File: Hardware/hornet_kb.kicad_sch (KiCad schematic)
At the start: 28 parts, among them J1 Conn_ST_STDC14, J10 USB_C_Receptacle_USB2.0, SW98 SW_Push, U1 nRF52840, Y1 32.768kHz, Y2 32MHz

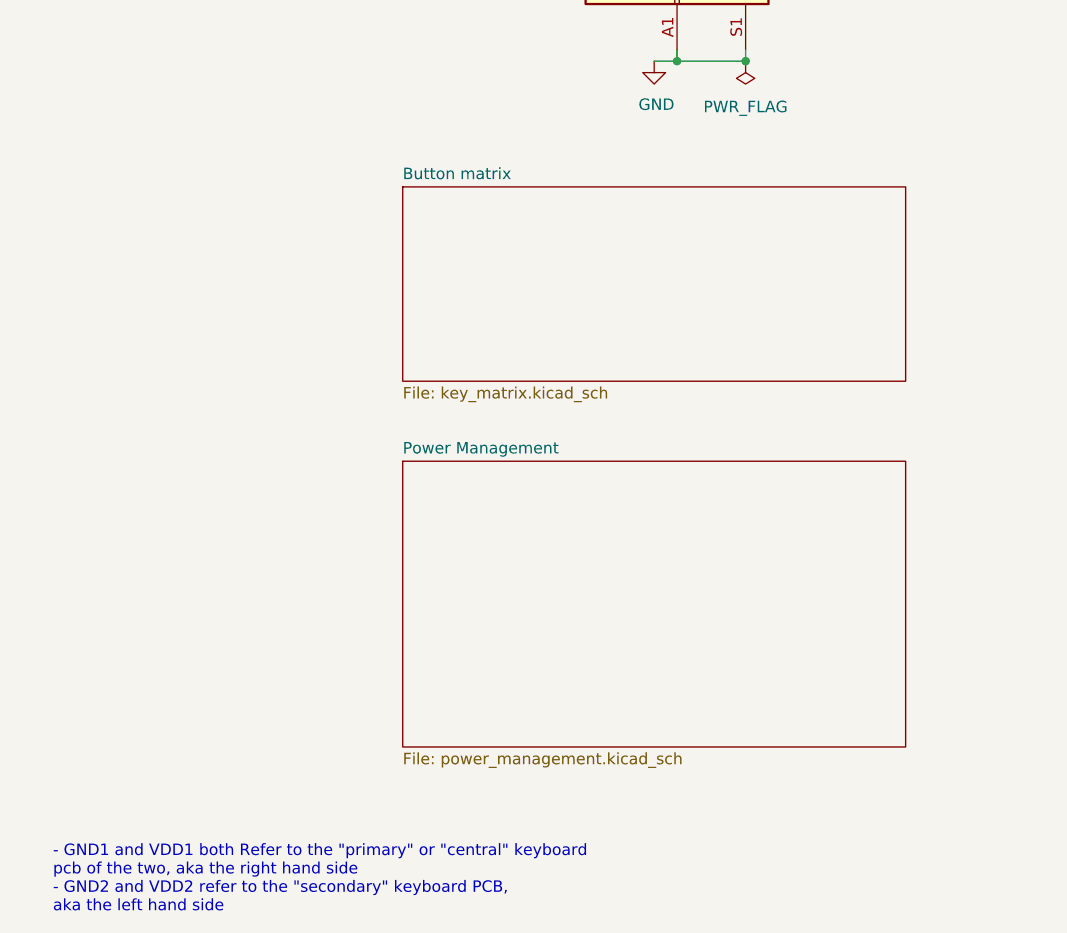
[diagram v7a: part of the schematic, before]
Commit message: Add higherarchical pins to key matrix
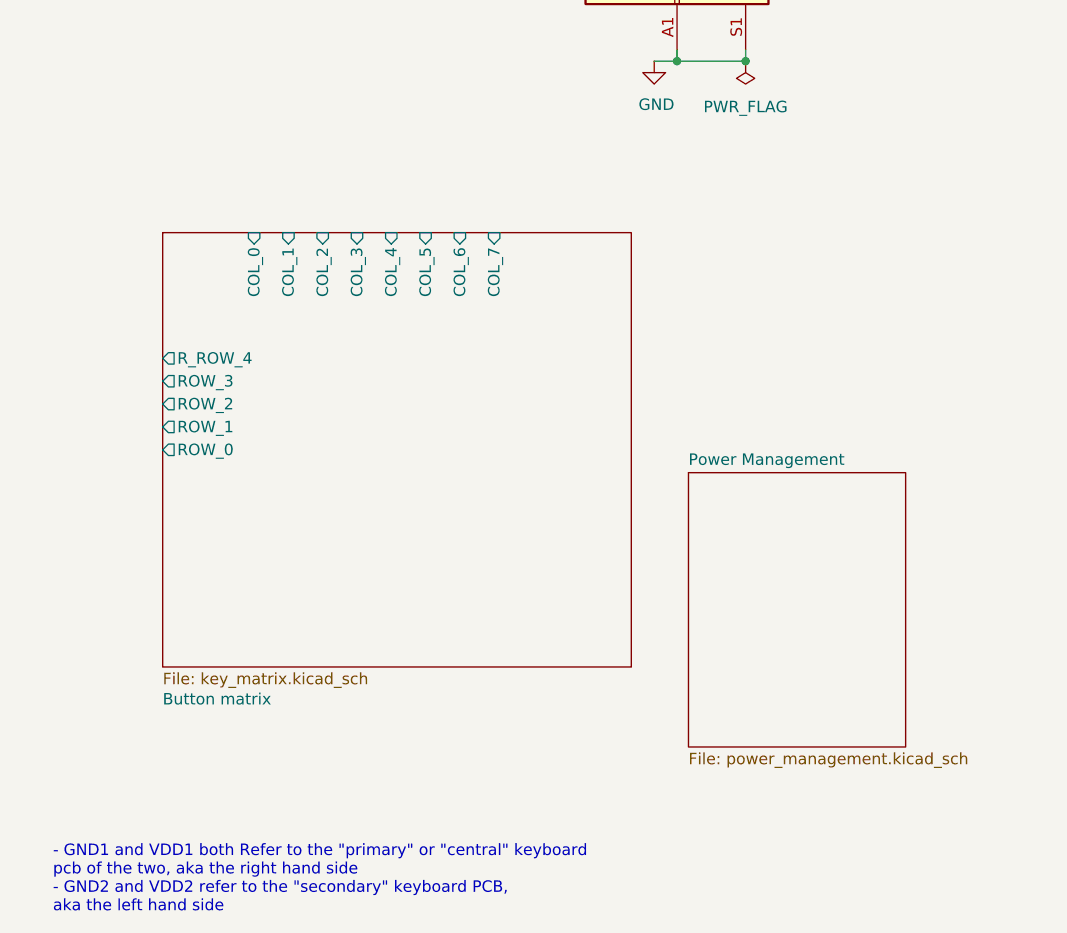
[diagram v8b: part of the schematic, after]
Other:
- sheet Button matrix ports: added COL_0, COL_1, COL_2, COL_3, COL_4, COL_5, COL_6, COL_7, ROW_0, ROW_1, ROW_2, ROW_3, R_ROW_4; removed none
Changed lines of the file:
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@@
 	)
 	(sheet
-		(at 241.3 167.64)
-		(size 55.88 31.75)
+		(at 273.05 168.91)
+		(size 24.13 30.48)
 		(exclude_from_sim no)
 		(in_bom yes)
@@
 		)
 		(property "Sheetname" "Power Management"
-			(at 241.3 166.9284 0)
+			(at 273.05 168.1984 0)
 			(effects
 				(font
@@
 		)
 		(property "Sheetfile" "power_management.kicad_sch"
-			(at 241.3 199.9746 0)
+			(at 273.05 199.9746 0)
 			(effects
 				(font
@@
 	)
 	(sheet
-		(at 241.3 137.16)
-		(size 55.88 21.59)
+		(at 214.63 142.24)
+		(size 52.07 48.26)
 		(exclude_from_sim no)
 		(in_bom yes)
 		(on_board yes)
 		(dnp no)
-		(fields_autoplaced yes)
 		(stroke
 			(width 0.1524)
@@
 		)
 		(property "Sheetname" "Button matrix"
-			(at 241.3 136.4484 0)
+			(at 214.63 194.818 0)
 			(effects
 				(font
@@
 		)
 		(property "Sheetfile" "key_matrix.kicad_sch"
-			(at 241.3 159.3346 0)
+			(at 214.63 191.0846 0)
 			(effects
 				(font
@@
 			)
 		)
+		(pin "COL_0" input
+			(at 224.79 142.24 90)
+			(effects
+				(font
+					(size 1.27 1.27)
+				)
+				(justify right)
+			)
+		)
+		(pin "COL_1" input
+			(at 228.6 142.24 90)
+			(effects
+				(font
+					(size 1.27 1.27)
+				)
+				(justify right)
+			)
+		)
+		(pin "COL_2" input
+			(at 232.41 142.24 90)
+			(effects
+				(font
+					(size 1.27 1.27)
+				)
+				(justify right)
+			)
+		)
+		(pin "COL_3" input
+			(at 236.22 142.24 90)
+			(effects
+				(font
+					(size 1.27 1.27)
+				)
+				(justify right)
+			)
+		)
+		(pin "COL_4" input
+			(at 240.03 142.24 90)
+			(effects
+				(font
+					(size 1.27 1.27)
+				)
+				(justify right)
+			)
+		)
+		(pin "COL_5" input
+			(at 243.84 142.24 90)
+			(effects
+				(font
+					(size 1.27 1.27)
+				)
+				(justify right)
+			)
+		)
+		(pin "COL_6" input
+			(at 247.65 142.24 90)
+			(effects
+				(font
+					(size 1.27 1.27)
+				)
+				(justify right)
+			)
+		)
+		(pin "COL_7" input
+			(at 251.46 142.24 90)
+			(effects
+				(font
+					(size 1.27 1.27)
+				)
+				(justify right)
+			)
+		)
+		(pin "ROW_0" output
+			(at 214.63 166.37 180)
+			(effects
+				(font
+					(size 1.27 1.27)
+				)
+				(justify left)
+			)
+		)
+		(pin "ROW_1" output
+			(at 214.63 163.83 180)
+			(effects
+				(font
+					(size 1.27 1.27)
+				)
+				(justify left)
+			)
+		)
+		(pin "ROW_2" output
+			(at 214.63 161.29 180)
+			(effects
+				(font
+					(size 1.27 1.27)
+				)
+				(justify left)
+			)
+		)
+		(pin "ROW_3" output
+			(at 214.63 158.75 180)
+			(effects
+				(font
+					(size 1.27 1.27)
+				)
+				(justify left)
+			)
+		)
+		(pin "R_ROW_4" output
+			(at 214.63 156.21 180)
+			(effects
+				(font
+					(size 1.27 1.27)
+				)
+				(justify left)
+			)
+		)
